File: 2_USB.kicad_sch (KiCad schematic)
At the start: 7 parts, among them J301 USB_C_Receptacle_USB2.0_16P, U301 CH224K, U303 USBLC6-2SC6, U304 USBLC6-2SC6

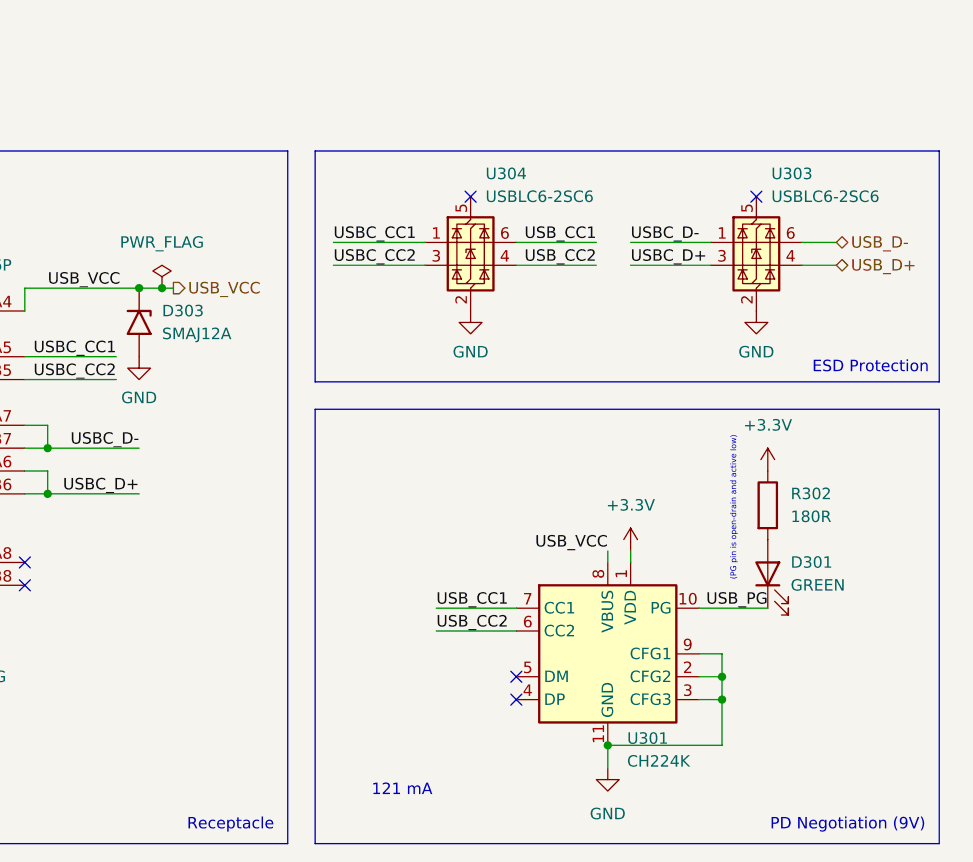
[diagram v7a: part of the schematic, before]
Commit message: Continued connections for the new NAV
Added continuity sensing through a 8:1 mux
Restructured schematic so that everything actually fits in page 4
Updated CubeMX (ioc) file with pinout
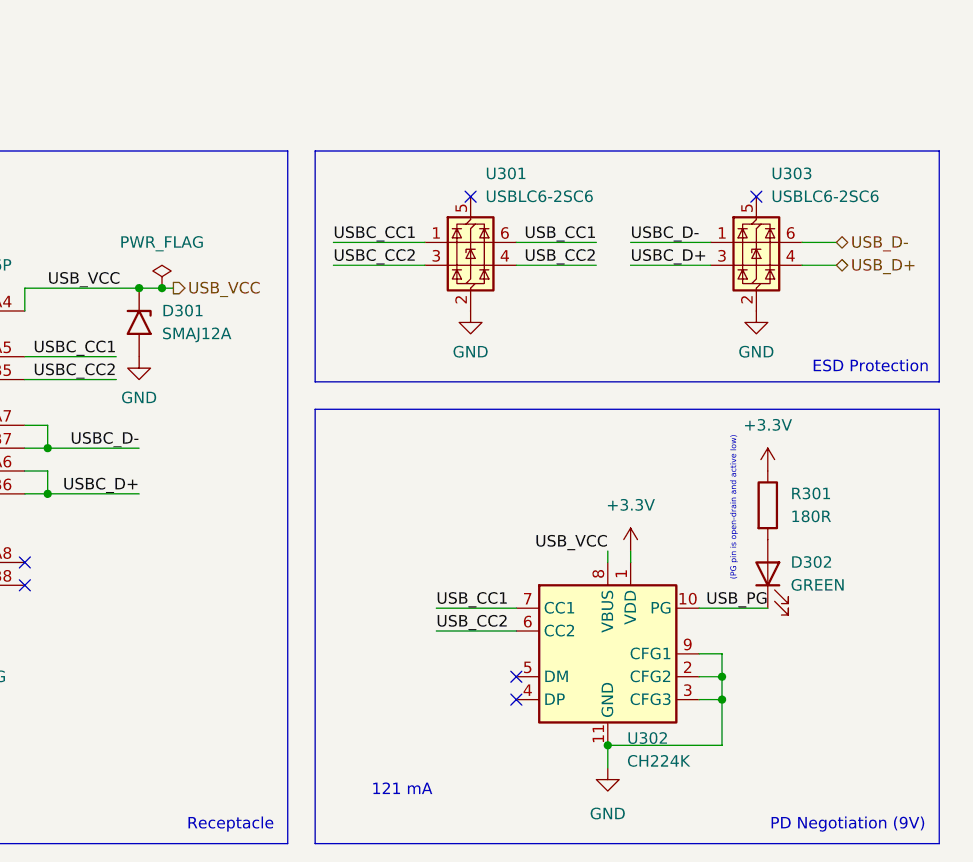
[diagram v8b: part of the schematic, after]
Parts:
- renumbered D303 to D301, D301 to D302, R302 to R301, U304 to U301, U301 to U302
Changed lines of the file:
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@@
 		(dnp no)
 		(fields_autoplaced yes)
-		(property "Reference" "D303"
+		(property "Reference" "D301"
 			(at 116.84 80.0099 90)
 			(show_name no)
@@
 			(project "polaris"
 				(path "/cfb90e19-9fbe-47a1-a5ac-df522853d1d0/f51c22fe-6c27-4a6e-b54b-9941150cfe5c"
-					(reference "D303")
+					(reference "D301")
 					(unit 1)
 				)
@@
 		(dnp no)
 		(fields_autoplaced yes)
-		(property "Reference" "#PWR0308"
+		(property "Reference" "#PWR0307"
 			(at 184.15 101.6 0)
 			(hide yes)
@@
 			(project "polaris"
 				(path "/cfb90e19-9fbe-47a1-a5ac-df522853d1d0/f51c22fe-6c27-4a6e-b54b-9941150cfe5c"
-					(reference "#PWR0308")
+					(reference "#PWR0307")
 					(unit 1)
 				)
@@
 		(dnp no)
 		(fields_autoplaced yes)
-		(property "Reference" "U304"
+		(property "Reference" "U301"
 			(at 152.7811 64.77 0)
 			(show_name no)
@@
 			(project "polaris"
 				(path "/cfb90e19-9fbe-47a1-a5ac-df522853d1d0/f51c22fe-6c27-4a6e-b54b-9941150cfe5c"
-					(reference "U304")
+					(reference "U301")
 					(unit 1)
 				)
@@
 		(dnp no)
 		(fields_autoplaced yes)
-		(property "Reference" "#FLG0301"
+		(property "Reference" "#FLG0302"
 			(at 116.84 75.565 0)
 			(hide yes)
@@
 			(project "polaris"
 				(path "/cfb90e19-9fbe-47a1-a5ac-df522853d1d0/f51c22fe-6c27-4a6e-b54b-9941150cfe5c"
-					(reference "#FLG0301")
+					(reference "#FLG0302")
 					(unit 1)
 				)
@@
 		(dnp no)
 		(fields_autoplaced yes)
-		(property "Reference" "#PWR0310"
+		(property "Reference" "#PWR0303"
 			(at 151.13 86.36 0)
 			(hide yes)
@@
 			(project "polaris"
 				(path "/cfb90e19-9fbe-47a1-a5ac-df522853d1d0/f51c22fe-6c27-4a6e-b54b-9941150cfe5c"
-					(reference "#PWR0310")
+					(reference "#PWR0303")
 					(unit 1)
 				)
@@
 		(dnp no)
 		(fields_autoplaced yes)
-		(property "Reference" "#PWR0303"
+		(property "Reference" "#PWR0302"
 			(at 114.3 91.44 0)
 			(hide yes)
@@
 			(project "polaris"
 				(path "/cfb90e19-9fbe-47a1-a5ac-df522853d1d0/f51c22fe-6c27-4a6e-b54b-9941150cfe5c"
-					(reference "#PWR0303")
+					(reference "#PWR0302")
 					(unit 1)
 				)
@@
 		(dnp no)
 		(fields_autoplaced yes)
-		(property "Reference" "R302"
+		(property "Reference" "R301"
 			(at 186.69 100.3299 0)
 			(show_name no)
@@
 			(project "polaris"
 				(path "/cfb90e19-9fbe-47a1-a5ac-df522853d1d0/f51c22fe-6c27-4a6e-b54b-9941150cfe5c"
-					(reference "R302")
+					(reference "R301")
 					(unit 1)
 				)
@@
 		(dnp no)
 		(fields_autoplaced yes)
-		(property "Reference" "#FLG0302"
+		(property "Reference" "#FLG0301"
 			(at 88.265 120.65 0)
 			(hide yes)
@@
 			(project "polaris"
 				(path "/cfb90e19-9fbe-47a1-a5ac-df522853d1d0/f51c22fe-6c27-4a6e-b54b-9941150cfe5c"
-					(reference "#FLG0302")
+					(reference "#FLG0301")
 					(unit 1)
 				)
@@
 		(dnp no)
 		(fields_autoplaced yes)
-		(property "Reference" "#PWR0307"
+		(property "Reference" "#PWR0305"
 			(at 168.91 110.49 0)
 			(hide yes)
@@
 			(project "polaris"
 				(path "/cfb90e19-9fbe-47a1-a5ac-df522853d1d0/f51c22fe-6c27-4a6e-b54b-9941150cfe5c"
-					(reference "#PWR0307")
+					(reference "#PWR0305")
 					(unit 1)
 				)
@@
 		(dnp no)
 		(fields_autoplaced yes)
-		(property "Reference" "U301"
+		(property "Reference" "U302"
 			(at 168.5133 127.508 0)
 			(show_name no)
@@
 			(project "polaris"
 				(path "/cfb90e19-9fbe-47a1-a5ac-df522853d1d0/f51c22fe-6c27-4a6e-b54b-9941150cfe5c"
-					(reference "U301")
+					(reference "U302")
 					(unit 1)
 				)
@@
 		(dnp no)
 		(fields_autoplaced yes)
-		(property "Reference" "#PWR0309"
+		(property "Reference" "#PWR0306"
 			(at 182.88 86.36 0)
 			(hide yes)
@@
 			(project "polaris"
 				(path "/cfb90e19-9fbe-47a1-a5ac-df522853d1d0/f51c22fe-6c27-4a6e-b54b-9941150cfe5c"
-					(reference "#PWR0309")
+					(reference "#PWR0306")
 					(unit 1)
 				)
@@
 		(in_pos_files yes)
 		(dnp no)
-		(property "Reference" "D301"
+		(property "Reference" "D302"
 			(at 186.69 107.95 90)
 			(show_name no)
@@
 			(project "polaris"
 				(path "/cfb90e19-9fbe-47a1-a5ac-df522853d1d0/f51c22fe-6c27-4a6e-b54b-9941150cfe5c"
-					(reference "D301")
+					(reference "D302")
 					(unit 1)
 				)
@@
 		(dnp no)
 		(fields_autoplaced yes)
-		(property "Reference" "#PWR0302"
+		(property "Reference" "#PWR0304"
 			(at 166.37 137.16 0)
 			(hide yes)
@@
 			(project "polaris"
 				(path "/cfb90e19-9fbe-47a1-a5ac-df522853d1d0/f51c22fe-6c27-4a6e-b54b-9941150cfe5c"
-					(reference "#PWR0302")
+					(reference "#PWR0304")
 					(unit 1)
 				)
